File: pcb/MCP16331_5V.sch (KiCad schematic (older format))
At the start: 11 parts, among them U8 MCP16331T

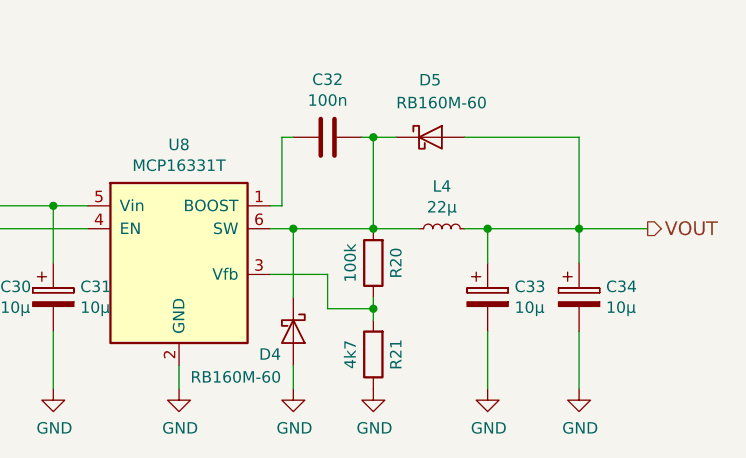
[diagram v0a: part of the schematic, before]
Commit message: Improve pcb routing, add testpoints and etc. The design improves a lot. Still lots to do, but most important design parts should now be drafted almost complete.
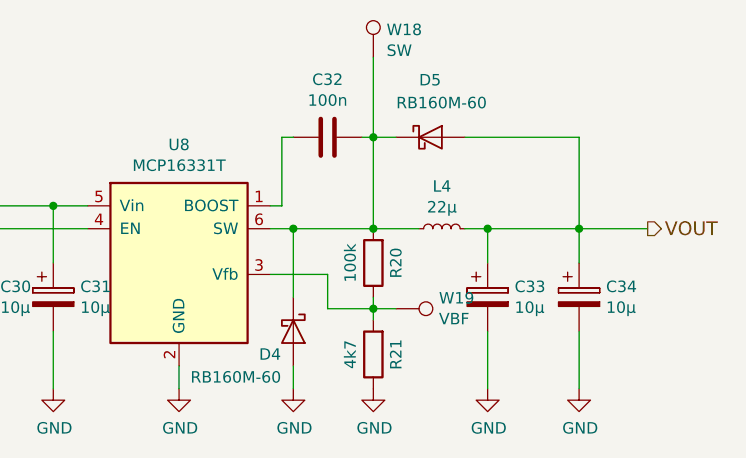
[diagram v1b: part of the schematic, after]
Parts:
- added W18: SW, Measurement_Points:Measurement_Point_Round-SMD-Pad_Small, symbol TEST_1P
- added W19: VBF, Measurement_Points:Measurement_Point_Round-SMD-Pad_Small, symbol TEST_1P
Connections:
- net at R20.1, R21.2, U8.3 (Vfb): now also W19.1
- net at C32.2, D4.1 (K), D5.1 (K)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: now also W18.1
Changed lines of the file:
@@
 $EndComp
 $Comp
-L GND #PWR069
+L GND #PWR082
 U 1 1 580BA37A
 P 5300 4150
-F 0 "#PWR069" H 5300 3900 50  0001 C CNN
+F 0 "#PWR082" H 5300 3900 50  0001 C CNN
 F 1 "GND" H 5305 3977 50  0000 C CNN
 F 2 "" H 5300 4150 50  0000 C CNN
@@
 $EndComp
 $Comp
-L GND #PWR070
+L GND #PWR083
 U 1 1 580BA3A1
 P 4750 4150
-F 0 "#PWR070" H 4750 3900 50  0001 C CNN
+F 0 "#PWR083" H 4750 3900 50  0001 C CNN
 F 1 "GND" H 4755 3977 50  0000 C CNN
 F 2 "" H 4750 4150 50  0000 C CNN
@@
 $EndComp
 $Comp
-L GND #PWR071
+L GND #PWR084
 U 1 1 580BA3A7
 P 4400 4150
-F 0 "#PWR071" H 4400 3900 50  0001 C CNN
+F 0 "#PWR084" H 4400 3900 50  0001 C CNN
 F 1 "GND" H 4405 3977 50  0000 C CNN
 F 2 "" H 4400 4150 50  0000 C CNN
@@
 	6100 3050 6250 3050
 Wire Wire Line
-	6150 3050 6150 3450
+	6150 2700 6150 3450
 Connection ~ 6150 3450
 Wire Wire Line
@@
 $EndComp
 $Comp
-L GND #PWR072
+L GND #PWR085
 U 1 1 580BA3CF
 P 6650 4150
-F 0 "#PWR072" H 6650 3900 50  0001 C CNN
+F 0 "#PWR085" H 6650 3900 50  0001 C CNN
 F 1 "GND" H 6655 3977 50  0000 C CNN
 F 2 "" H 6650 4150 50  0000 C CNN
@@
 $EndComp
 $Comp
-L GND #PWR073
+L GND #PWR086
 U 1 1 580BA3D5
 P 7050 4150
-F 0 "#PWR073" H 7050 3900 50  0001 C CNN
+F 0 "#PWR086" H 7050 3900 50  0001 C CNN
 F 1 "GND" H 7055 3977 50  0000 C CNN
 F 2 "" H 7050 4150 50  0000 C CNN
@@
 $EndComp
 $Comp
-L GND #PWR074
+L GND #PWR087
 U 1 1 580BA3EB
 P 6150 4150
-F 0 "#PWR074" H 6150 3900 50  0001 C CNN
+F 0 "#PWR087" H 6150 3900 50  0001 C CNN
 F 1 "GND" H 6155 3977 50  0000 C CNN
 F 2 "" H 6150 4150 50  0000 C CNN
@@
 	5950 3650 5950 3800
 Wire Wire Line
-	5950 3800 6150 3800
+	5950 3800 6250 3800
 Connection ~ 6150 3800
 $Comp
@@
 Connection ~ 5800 3450
 $Comp
-L GND #PWR075
+L GND #PWR088
 U 1 1 580BA3FF
 P 5800 4150
-F 0 "#PWR075" H 5800 3900 50  0001 C CNN
+F 0 "#PWR088" H 5800 3900 50  0001 C CNN
 F 1 "GND" H 5805 3977 50  0000 C CNN
 F 2 "" H 5800 4150 50  0000 C CNN
@@
 Text HLabel 4250 3450 0    60   Input ~ 0
 EN
+$Comp
+L TEST_1P W19
+U 1 1 58179C3A
+P 6250 3800
+F 0 "W19" V 6204 3987 50  0000 L CNN
+F 1 "VBF" V 6295 3987 50  0000 L CNN
+F 2 "Measurement_Points:Measurement_Point_Round-SMD-Pad_Small" H 6450 3800 50  0001 C CNN
+F 3 "" H 6450 3800 50  0000 C CNN
+	1    6250 3800
+	0    1    1    0
+$EndComp
+$Comp
+L TEST_1P W18
+U 1 1 5817A2DF
+P 6150 2700
+F 0 "W18" H 6208 2820 50  0000 L CNN
+F 1 "SW" H 6208 2729 50  0000 L CNN
+F 2 "Measurement_Points:Measurement_Point_Round-SMD-Pad_Small" H 6350 2700 50  0001 C CNN
+F 3 "" H 6350 2700 50  0000 C CNN
+	1    6150 2700
+	1    0    0    -1
+$EndComp
 $EndSCHEMATC

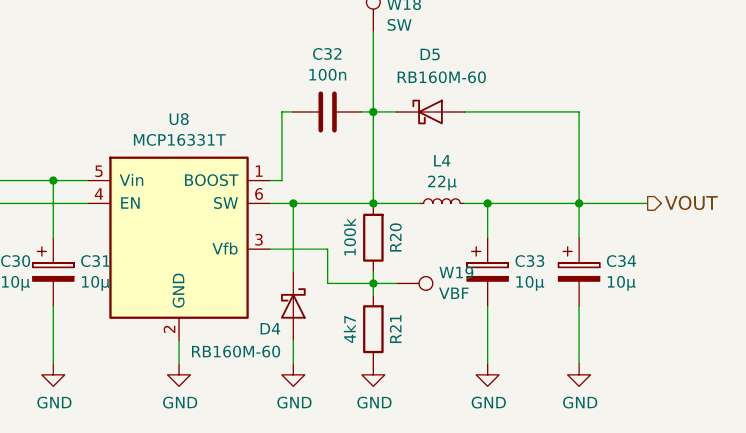
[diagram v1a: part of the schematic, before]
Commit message: Improve board routing, add some dukos
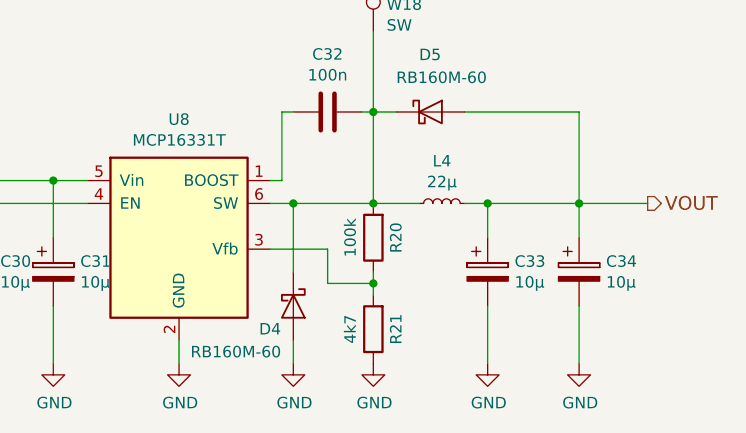
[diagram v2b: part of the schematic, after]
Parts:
- removed W19: VBF, Measurement_Points:Measurement_Point_Round-SMD-Pad_Small, symbol TEST_1P
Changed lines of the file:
@@
 Wire Wire Line
 	5950 3650 5950 3800
-Wire Wire Line
-	5950 3800 6250 3800
 Connection ~ 6150 3800
 $Comp
@@
 EN
 $Comp
-L TEST_1P W19
-U 1 1 58179C3A
-P 6250 3800
-F 0 "W19" V 6204 3987 50  0000 L CNN
-F 1 "VBF" V 6295 3987 50  0000 L CNN
-F 2 "Measurement_Points:Measurement_Point_Round-SMD-Pad_Small" H 6450 3800 50  0001 C CNN
-F 3 "" H 6450 3800 50  0000 C CNN
-	1    6250 3800
-	0    1    1    0
-$EndComp
-$Comp
 L TEST_1P W18
 U 1 1 5817A2DF
@@
 	1    0    0    -1
 $EndComp
+Wire Wire Line
+	5950 3800 6150 3800
 $EndSCHEMATC

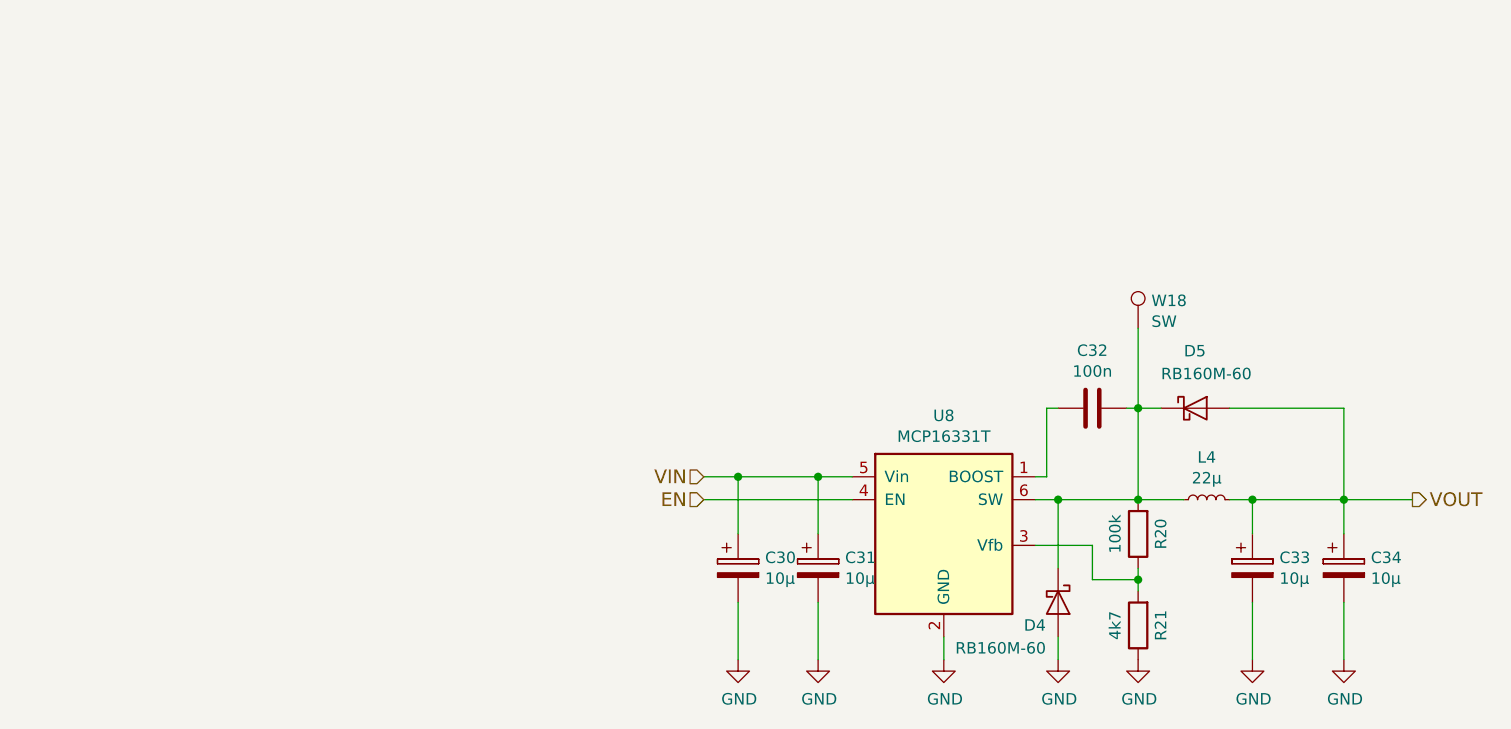
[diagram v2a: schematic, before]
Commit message: Add some little changes to the schematic, add calculations
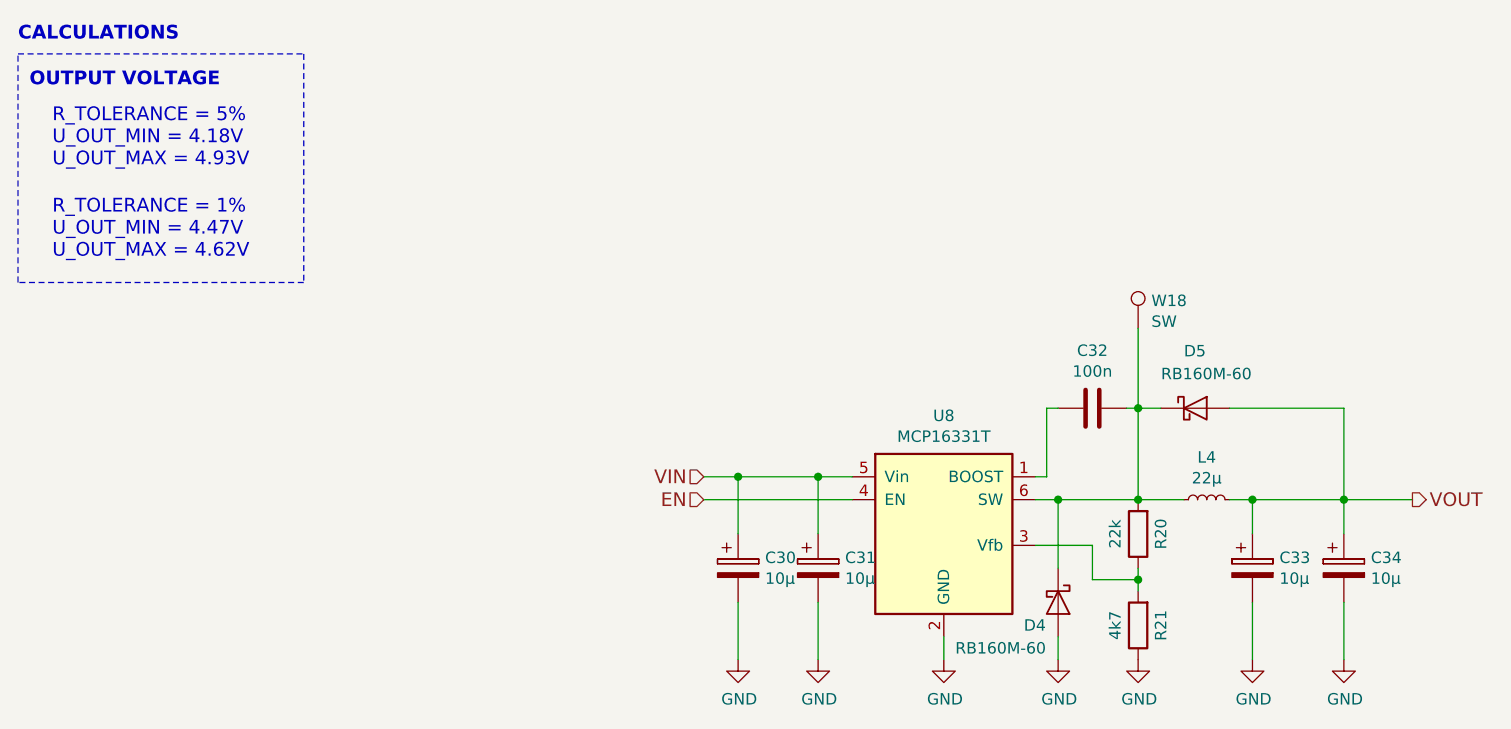
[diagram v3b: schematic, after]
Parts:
- R20: value 100k -> 22k
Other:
- note added: "CALCULATIONS"
- note added: "OUTPUT VOLTAGE"
- note added: "R_TOLERANCE = 1%\nU_OUT_MIN = 4.47V\nU_OUT_MAX = 4.62V"
- note added: "R_TOLERANCE = 5%\nU_OUT_MIN = 4.18V\nU_OUT_MAX = 4.93V"
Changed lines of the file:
@@
 $EndComp
 $Comp
-L GND #PWR082
+L GND #PWR083
 U 1 1 580BA37A
 P 5300 4150
-F 0 "#PWR082" H 5300 3900 50  0001 C CNN
+F 0 "#PWR083" H 5300 3900 50  0001 C CNN
 F 1 "GND" H 5305 3977 50  0000 C CNN
 F 2 "" H 5300 4150 50  0000 C CNN
@@
 $EndComp
 $Comp
-L GND #PWR083
+L GND #PWR084
 U 1 1 580BA3A1
 P 4750 4150
-F 0 "#PWR083" H 4750 3900 50  0001 C CNN
+F 0 "#PWR084" H 4750 3900 50  0001 C CNN
 F 1 "GND" H 4755 3977 50  0000 C CNN
 F 2 "" H 4750 4150 50  0000 C CNN
@@
 $EndComp
 $Comp
-L GND #PWR084
+L GND #PWR085
 U 1 1 580BA3A7
 P 4400 4150
-F 0 "#PWR084" H 4400 3900 50  0001 C CNN
+F 0 "#PWR085" H 4400 3900 50  0001 C CNN
 F 1 "GND" H 4405 3977 50  0000 C CNN
 F 2 "" H 4400 4150 50  0000 C CNN
@@
 $EndComp
 $Comp
-L GND #PWR085
+L GND #PWR086
 U 1 1 580BA3CF
 P 6650 4150
-F 0 "#PWR085" H 6650 3900 50  0001 C CNN
+F 0 "#PWR086" H 6650 3900 50  0001 C CNN
 F 1 "GND" H 6655 3977 50  0000 C CNN
 F 2 "" H 6650 4150 50  0000 C CNN
@@
 $EndComp
 $Comp
-L GND #PWR086
+L GND #PWR087
 U 1 1 580BA3D5
 P 7050 4150
-F 0 "#PWR086" H 7050 3900 50  0001 C CNN
+F 0 "#PWR087" H 7050 3900 50  0001 C CNN
 F 1 "GND" H 7055 3977 50  0000 C CNN
 F 2 "" H 7050 4150 50  0000 C CNN
@@
 P 6150 3600
 F 0 "R20" V 6050 3600 50  0000 C CNN
-F 1 "100k" V 6250 3600 50  0000 C CNN
+F 1 "22k" V 6250 3600 50  0000 C CNN
 F 2 "Resistors_SMD:R_0603" V 6080 3600 50  0001 C CNN
 F 3 "" H 6150 3600 50  0000 C CNN
@@
 $EndComp
 $Comp
-L GND #PWR087
+L GND #PWR088
 U 1 1 580BA3EB
 P 6150 4150
-F 0 "#PWR087" H 6150 3900 50  0001 C CNN
+F 0 "#PWR088" H 6150 3900 50  0001 C CNN
 F 1 "GND" H 6155 3977 50  0000 C CNN
 F 2 "" H 6150 4150 50  0000 C CNN
@@
 Connection ~ 5800 3450
 $Comp
-L GND #PWR088
+L GND #PWR089
 U 1 1 580BA3FF
 P 5800 4150
-F 0 "#PWR088" H 5800 3900 50  0001 C CNN
+F 0 "#PWR089" H 5800 3900 50  0001 C CNN
 F 1 "GND" H 5805 3977 50  0000 C CNN
 F 2 "" H 5800 4150 50  0000 C CNN
@@
 Wire Wire Line
 	5950 3800 6150 3800
+Text Notes 1250 1450 0    60   ~ 12
+CALCULATIONS
+Text Notes 1400 2000 0    60   ~ 0
+R_TOLERANCE = 5%\nU_OUT_MIN = 4.18V\nU_OUT_MAX = 4.93V
+Text Notes 1400 2400 0    60   ~ 0
+R_TOLERANCE = 1%\nU_OUT_MIN = 4.47V\nU_OUT_MAX = 4.62V
+Text Notes 1300 1650 0    60   ~ 12
+OUTPUT VOLTAGE
+Wire Notes Line
+	1250 1500 2500 1500
+Wire Notes Line
+	2500 1500 2500 2500
+Wire Notes Line
+	2500 2500 1250 2500
+Wire Notes Line
+	1250 2500 1250 1500
 $EndSCHEMATC

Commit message: Add some digikey order informations to components
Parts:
- L4: Digi-Key Minimum Quantity (none) -> 1; Digi-Key Part Number (none) -> 732-1258-1-ND
- U8: Digi-Key Minimum Quantity (none) -> 1; Digi-Key Part Number (none) -> MCP16331T-E/CHCT-ND
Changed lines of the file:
@@
 F 1 "MCP16331T" H 5300 4126 50  0000 C CNN
 F 2 "TO_SOT_Packages_SMD:SOT-23-6" H 5300 3150 50  0001 C CNN
-F 3 "" H 5000 4200 50  0000 C CNN
+F 3 "http://ww1.microchip.com/downloads/en/DeviceDoc/20005308B.pdf" H 5000 4200 50  0001 C CNN
+F 4 "MCP16331T-E/CHCT-ND" H 5300 3650 60  0001 C CNN "Digi-Key Part Number"
+F 5 "1" H 5300 3650 60  0001 C CNN "Digi-Key Minimum Quantity"
 	1    5300 3650
 	1    0    0    -1
@@
 F 1 "22µ" V 6544 3450 50  0000 C CNN
 F 2 "Inductors_local:Inductor_Würth_SPC_4818" H 6450 3450 50  0001 C CNN
-F 3 "" H 6450 3450 50  0000 C CNN
+F 3 "http://katalog.we-online.de/pbs/datasheet/744773122.pdf" H 6450 3450 50  0001 C CNN
+F 4 "732-1258-1-ND" V 6450 3450 60  0001 C CNN "Digi-Key Part Number"
+F 5 "1" V 6450 3450 60  0001 C CNN "Digi-Key Minimum Quantity"
 	1    6450 3450
 	0    -1   -1   0

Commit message: Add more BOM informations
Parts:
- C32: Digi-Key Minimum Quantity (none) -> 1; Digi-Key Part Number (none) -> 311-1343-1-ND
- R20: Digi-Key Minimum Quantity (none) -> 5000; Digi-Key Part Number (none) -> 311-22.0KHRTR-ND
- R21: Digi-Key Minimum Quantity (none) -> 5000; Digi-Key Part Number (none) -> 311-4.70KHRTR-ND
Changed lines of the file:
@@
 F 2 "Capacitors_SMD:C_0603" H 5988 2900 50  0001 C CNN
 F 3 "" H 5950 3050 50  0000 C CNN
+F 4 "311-1343-1-ND" H 5950 3050 60  0001 C CNN "Digi-Key Part Number"
+F 5 "1" H 5950 3050 60  0001 C CNN "Digi-Key Minimum Quantity"
 	1    5950 3050
 	0    -1   -1   0
@@
 F 2 "Resistors_SMD:R_0603" V 6080 3600 50  0001 C CNN
 F 3 "" H 6150 3600 50  0000 C CNN
+F 4 "311-22.0KHRTR-ND" H 6150 3600 60  0001 C CNN "Digi-Key Part Number"
+F 5 "5000" H 6150 3600 60  0001 C CNN "Digi-Key Minimum Quantity"
 	1    6150 3600
 	-1   0    0    1
@@
 F 2 "Resistors_SMD:R_0603" V 6080 4000 50  0001 C CNN
 F 3 "" H 6150 4000 50  0000 C CNN
+F 4 "311-4.70KHRTR-ND" H 6150 4000 60  0001 C CNN "Digi-Key Part Number"
+F 5 "5000" H 6150 4000 60  0001 C CNN "Digi-Key Minimum Quantity"
 	1    6150 4000
 	-1   0    0    1

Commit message: Improve BOM
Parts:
- R20: Digi-Key Minimum Quantity 5000 -> 1; Digi-Key Part Number 311-22.0KHRTR-ND -> 311-22.0KHRCT-ND
- R21: Digi-Key Minimum Quantity 5000 -> 1; Digi-Key Part Number 311-4.70KHRTR-ND -> 311-4.70KHRCT-ND
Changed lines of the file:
@@
 F 2 "Resistors_SMD:R_0603" V 6080 3600 50  0001 C CNN
 F 3 "" H 6150 3600 50  0000 C CNN
-F 4 "311-22.0KHRTR-ND" H 6150 3600 60  0001 C CNN "Digi-Key Part Number"
-F 5 "5000" H 6150 3600 60  0001 C CNN "Digi-Key Minimum Quantity"
+F 4 "311-22.0KHRCT-ND" H 6150 3600 60  0001 C CNN "Digi-Key Part Number"
+F 5 "1" H 6150 3600 60  0001 C CNN "Digi-Key Minimum Quantity"
 	1    6150 3600
 	-1   0    0    1
@@
 F 2 "Resistors_SMD:R_0603" V 6080 4000 50  0001 C CNN
 F 3 "" H 6150 4000 50  0000 C CNN
-F 4 "311-4.70KHRTR-ND" H 6150 4000 60  0001 C CNN "Digi-Key Part Number"
-F 5 "5000" H 6150 4000 60  0001 C CNN "Digi-Key Minimum Quantity"
+F 4 "311-4.70KHRCT-ND" H 6150 4000 60  0001 C CNN "Digi-Key Part Number"
+F 5 "1" H 6150 4000 60  0001 C CNN "Digi-Key Minimum Quantity"
 	1    6150 4000
 	-1   0    0    1
